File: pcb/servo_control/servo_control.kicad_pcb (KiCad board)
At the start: 2 copper layers, 23 parts, among them J1 USB_B_Micro, J10 Conn_01x03_Female, J11 Conn_01x03_Female, J12 Conn_01x03_Female, J13 Conn_01x03_Female, J14 Conn_01x03_Female, J15 Conn_01x03_Female, J16 Conn_01x03_Female, J17 Conn_01x03_Female, J18 Conn_01x03_Female, J19 Conn_01x03_Female, J2 Conn_02x03_Counter_Clockwise, J20 Conn_01x03_Female, J3 Conn_01x03_Female, J4 Conn_01x03_Female, J5 Conn_01x03_Female, J6 Conn_01x03_Female, J7 Conn_01x03_Female, J8 Conn_01x03_Female, J9 Conn_01x03_Female, U1 ATmega2560-16A, U2 MCP73832-2-OT

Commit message: add ftdi
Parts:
- added C1: 1 uf, Capacitor_SMD:C_0603_1608Metric, F.Cu at (109.2, 83.8)
- added C2: 1uf, Capacitor_SMD:C_0603_1608Metric, F.Cu at (119.4, 78.7)
- added C3: 10 uf, Capacitor_SMD:C_0603_1608Metric, F.Cu at (119.4, 81.3)
- added U3: ESP32-WROOM-32, ESP32:MODULE_ESP32-WROOM-32, F.Cu at (106.7, 63.5)
- U2: value MCP73832-2-OT -> LM317_SOT-223; footprint Package_TO_SOT_SMD:SOT-23-5 -> Package_TO_SOT_SMD:SOT-223-3_TabPin2
- moved U2 76.1 mm to (112.4, 78.7)
- moved J12 66.5 mm to (182.6, 96.8)
- moved J7 66.3 mm to (147.3, 43.2)
- moved J13 65.2 mm to (185.2, 96.8)
- moved J10 54.0 mm to (185.4, 43.2)
- moved J9 53.3 mm to (182.9, 43.2)
- moved D1 53.1 mm to (102.3, 75.2), turned to 180 degrees
- moved J14 51.8 mm to (187.7, 96.8)
- moved J18 32.7 mm to (149.8, 96.8)
- moved J15 31.9 mm to (104.1, 96.5)
- moved J17 31.4 mm to (109.2, 96.5)
- moved J2 30.9 mm to (132.1, 86.4), turned to 90 degrees
- moved J8 25.1 mm to (149.9, 43.2)
- moved U1 24.4 mm to (147.3, 73.7)
- moved J20 23.0 mm to (144.8, 96.8)
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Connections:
- net MISO renamed GPIO_50
- net SCK renamed GPIO_52
- J10 pad 3: unconnected-(J10-Pad3) -> GPIO_33
- J11 pad 3: unconnected-(J11-Pad3) -> GPIO_35
- J12 pad 3: unconnected-(J12-Pad3) -> GPIO_37
- J13 pad 3: unconnected-(J13-Pad3) -> GPIO_39
- J14 pad 3: unconnected-(J14-Pad3) -> GPIO_41
- J15 pad 3: unconnected-(J15-Pad3) -> GPIO_49
- J16 pad 3: unconnected-(J16-Pad3) -> GPIO_51
- J17 pad 3: unconnected-(J17-Pad3) -> GPIO_53
- J18 pad 3: unconnected-(J18-Pad3) -> GPIO_43
- J19 pad 3: unconnected-(J19-Pad3) -> GPIO_45
- J2 pad 5: MOSI -> GPIO_51
- J20 pad 3: unconnected-(J20-Pad3) -> GPIO_47
- J9 pad 3: unconnected-(J9-Pad3) -> GPIO_31
- U1 pad 11: Net-(U1-Pad11) -> GND
- U1 pad 21: MOSI -> GPIO_51
- U1 pad 32: Net-(U1-Pad11) -> GND
- U1 pad 43: unconnected-(U1-Pad43) -> GPIO_21
- U1 pad 44: unconnected-(U1-Pad44) -> GPIO_20
- U1 pad 45: unconnected-(U1-Pad45) -> GPIO_19
- U1 pad 46: unconnected-(U1-Pad46) -> GPIO_18
- U1 pad 50: unconnected-(U1-Pad50) -> GPIO_38
- U1 pad 53: unconnected-(U1-Pad53) -> GPIO_37
- U1 pad 54: unconnected-(U1-Pad54) -> GPIO_36
- U1 pad 55: unconnected-(U1-Pad55) -> GPIO_35
- U1 pad 56: unconnected-(U1-Pad56) -> GPIO_34
- U1 pad 57: unconnected-(U1-Pad57) -> GPIO_33
- U1 pad 58: unconnected-(U1-Pad58) -> GPIO_32
- U1 pad 59: unconnected-(U1-Pad59) -> GPIO_31
- U1 pad 60: unconnected-(U1-Pad60) -> GPIO_30
- U1 pad 62: Net-(U1-Pad11) -> GND
- U1 pad 81: Net-(U1-Pad11) -> GND
- U1 pad 82: unconnected-(U1-Pad82) -> GPIO_15
- U1 pad 83: unconnected-(U1-Pad83) -> GPIO_14
- U1 pad 84: unconnected-(U1-Pad84) -> GPIO_13
- U1 pad 85: unconnected-(U1-Pad85) -> GPIO_12
- U1 pad 86: unconnected-(U1-Pad86) -> GPIO_11
- U1 pad 87: unconnected-(U1-Pad87) -> GPIO_10
- U1 pad 88: unconnected-(U1-Pad88) -> GPIO_9
- U1 pad 89: unconnected-(U1-Pad89) -> GPIO_8
- U1 pad 90: unconnected-(U1-Pad90) -> GPIO_7
- U1 pad 91: unconnected-(U1-Pad91) -> GPIO_6
- U1 pad 92: unconnected-(U1-Pad92) -> GPIO_5
- U1 pad 93: unconnected-(U1-Pad93) -> GPIO_4
- U1 pad 94: unconnected-(U1-Pad94) -> GPIO_3
- U1 pad 95: unconnected-(U1-Pad95) -> GPIO_2
- U1 pad 96: unconnected-(U1-Pad96) -> GPIO_1
- U1 pad 97: unconnected-(U1-Pad97) -> GPIO_0
- U1 pad 99: Net-(U1-Pad11) -> GND
- U2 pad 1: unconnected-(U2-Pad1) -> GND
- U2 pad 2: unconnected-(U2-Pad2) -> 3.3V
- U2 pad 3: unconnected-(U2-Pad3) -> VCC

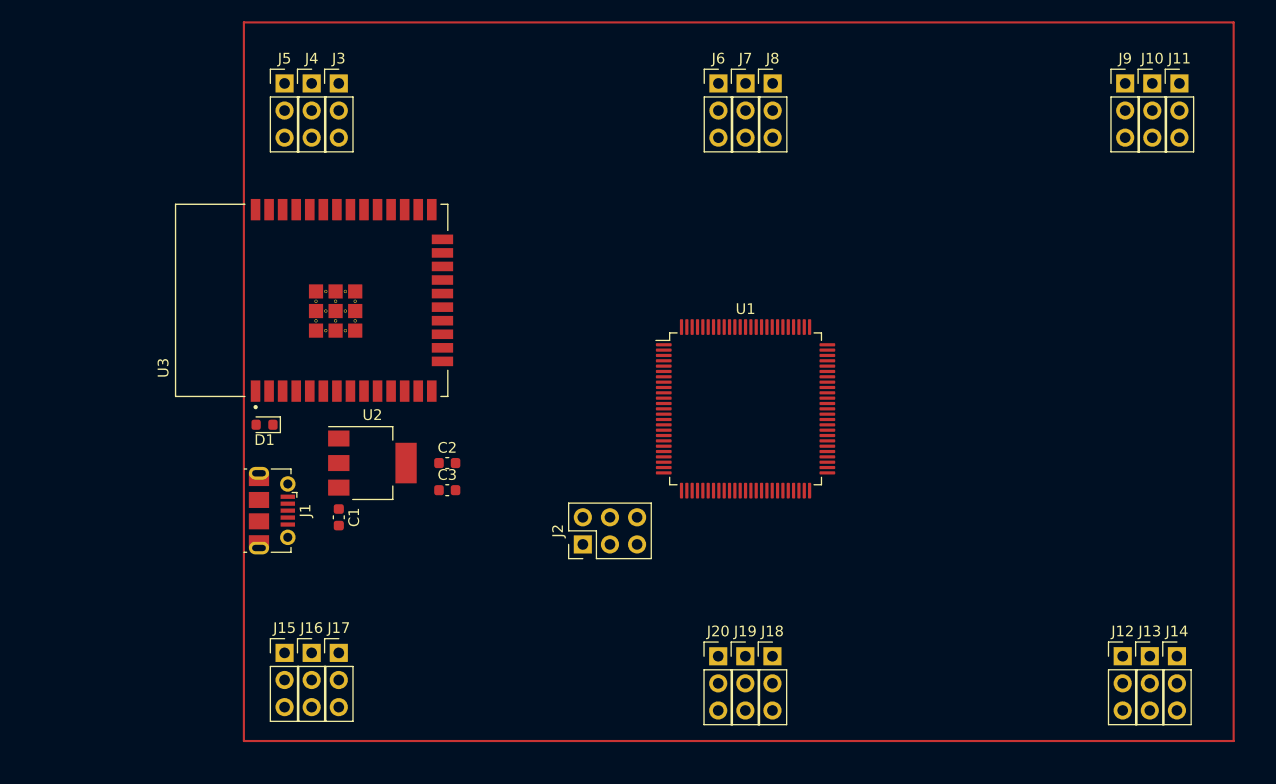
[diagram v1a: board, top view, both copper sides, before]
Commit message: add i2c
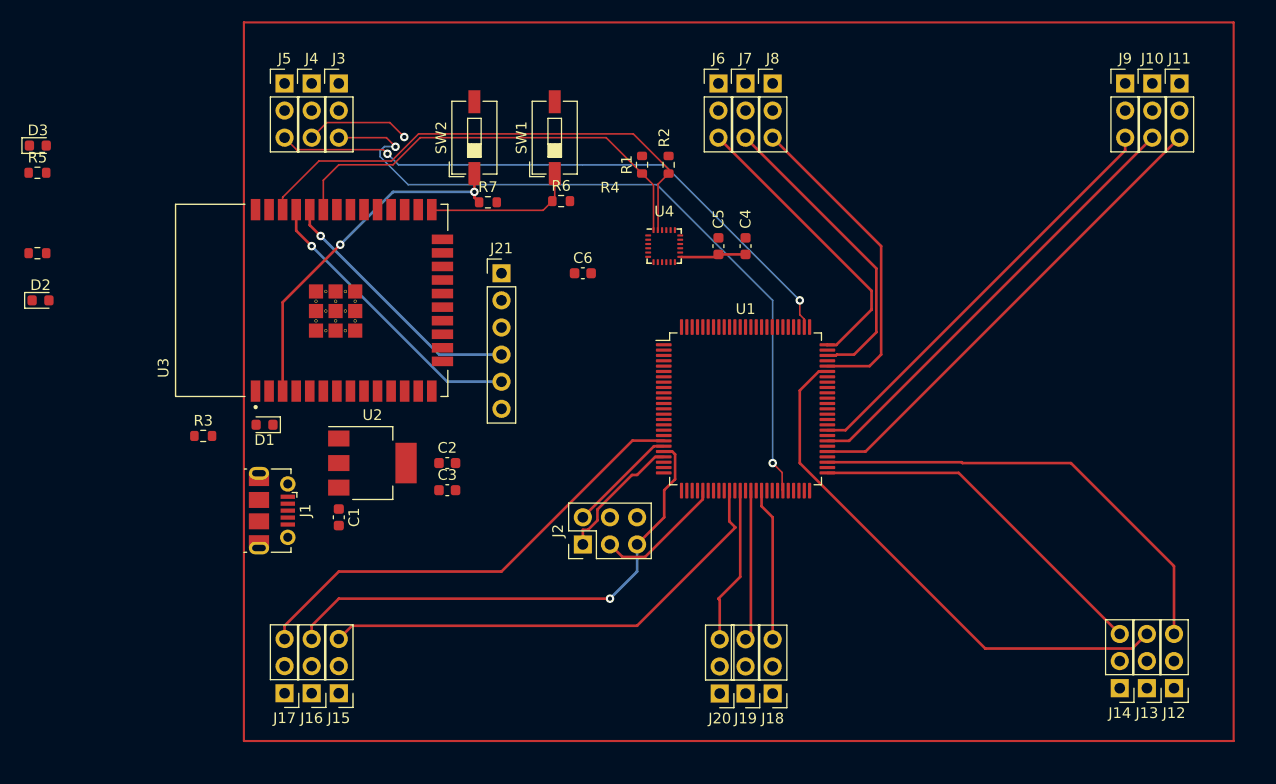
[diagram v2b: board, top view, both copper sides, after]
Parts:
- added C4: 10 nf, Capacitor_SMD:C_0603_1608Metric, F.Cu at (147.3, 58.4)
- added C5: 0.1 uf, Capacitor_SMD:C_0603_1608Metric, F.Cu at (144.8, 58.4)
- added C6: 0.1 uf, Capacitor_SMD:C_0603_1608Metric, F.Cu at (132.1, 61.0)
- added D2: LED, LED_SMD:LED_0603_1608Metric, F.Cu at (81.3, 63.5)
- added D3: LED, LED_SMD:LED_0603_1608Metric, F.Cu at (81.0, 49.0)
- added J21: Conn_01x06_Male, Connector_PinHeader_2.54mm:PinHeader_1x06_P2.54mm_Vertical, F.Cu at (124.5, 61.0)
- added R1: 4.7K, Resistor_SMD:R_0603_1608Metric, F.Cu at (137.6, 50.8)
- added R2: 4.7K, Resistor_SMD:R_0603_1608Metric, F.Cu at (140.1, 50.8)
- added R3: 1K, Resistor_SMD:R_0603_1608Metric, F.Cu at (96.5, 76.2)
- added R4: 1K, Resistor_SMD:R_0603_1608Metric, F.Cu at (81.0, 59.1)
- added R5: 1K, Resistor_SMD:R_0603_1608Metric, F.Cu at (81.0, 51.5)
- added R6: 10K, Resistor_SMD:R_0603_1608Metric, F.Cu at (130.0, 54.2)
- added R7: 10K, Resistor_SMD:R_0603_1608Metric, F.Cu at (123.2, 54.3)
- added SW1: ESP_PROG, Button_Switch_SMD:SW_DIP_SPSTx01_Slide_6.7x4.1mm_W6.73mm_P2.54mm_LowProfile_JPin, F.Cu at (129.4, 48.3)
- added SW2: ESP_RST, Button_Switch_SMD:SW_DIP_SPSTx01_Slide_6.7x4.1mm_W6.73mm_P2.54mm_LowProfile_JPin, F.Cu at (121.9, 48.3)
- added U4: MPU-9250, Sensor_Motion:InvenSense_QFN-24_3x3mm_P0.4mm, F.Cu at (139.7, 58.4)
- moved J15 6.33 mm to (109.2, 100.3), turned to 180 degrees
- moved J17 6.33 mm to (104.1, 100.3), turned to 180 degrees
- moved J14 6.14 mm to (182.4, 99.8), turned to 180 degrees
- moved J12 5.66 mm to (187.5, 99.8), turned to 180 degrees
- moved J16 3.78 mm to (106.7, 100.3), turned to 180 degrees
- moved J20 3.50 mm to (144.9, 100.3), turned to 180 degrees
- moved J18 3.50 mm to (149.9, 100.3), turned to 180 degrees
- moved J19 3.50 mm to (147.3, 100.3), turned to 180 degrees
- moved J13 3.01 mm to (184.9, 99.8), turned to 180 degrees
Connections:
- D1 pad 1: unconnected-(D1-Pad1) -> GND
- D1 pad 2: unconnected-(D1-Pad2) -> Net-(D1-Pad2)
- J1 pad 6: unconnected-(J1-Pad6) -> GND
- U1 pad 35: unconnected-(U1-Pad35) -> GPIO_49
- U1 pad 36: unconnected-(U1-Pad36) -> GPIO_48
- U1 pad 37: unconnected-(U1-Pad37) -> GPIO_47
- U1 pad 38: unconnected-(U1-Pad38) -> GPIO_46
- U1 pad 39: unconnected-(U1-Pad39) -> GPIO_45
- U1 pad 40: unconnected-(U1-Pad40) -> GPIO_44
- U1 pad 41: unconnected-(U1-Pad41) -> GPIO_43
- U1 pad 42: unconnected-(U1-Pad42) -> GPIO_42
- U1 pad 43: GPIO_21 -> I2C_SCL
- U1 pad 44: GPIO_20 -> I2C_SDA
- U1 pad 51: unconnected-(U1-Pad51) -> GPIO_41
- U1 pad 52: unconnected-(U1-Pad52) -> GPIO_40
- U1 pad 70: unconnected-(U1-Pad70) -> GPIO_39
- U3 pad 2: unconnected-(U3-Pad2) -> 3.3V
- U3 pad 25: unconnected-(U3-Pad25) -> Net-(U3-Pad25)
- U3 pad 3: unconnected-(U3-Pad3) -> Net-(U3-Pad3)
- U3 pad 33: unconnected-(U3-Pad33) -> I2C_SDA
- U3 pad 34: unconnected-(U3-Pad34) -> FTDI_TX
- U3 pad 35: unconnected-(U3-Pad35) -> FTDI_RX
- U3 pad 36: unconnected-(U3-Pad36) -> I2C_SCL
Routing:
- net GPIO_19: track 0.00 -> 68.4 mm, vias 0 -> 2
- net GPIO_23: track 0.00 -> 57.2 mm, vias 0 -> 2
- net GPIO_39: track 0.00 -> 50.4 mm
- net GPIO_51: track 0.00 -> 47.4 mm, vias 0 -> 1
- net I2C_SCL: track 0.00 -> 47.3 mm
- net GPIO_49: track 0.00 -> 45.3 mm
- net GPIO_35: track 0.00 -> 45.2 mm
- net GPIO_53: track 0.00 -> 44.0 mm
- net GPIO_37: track 0.00 -> 42.9 mm
- net GPIO_33: track 0.00 -> 42.2 mm
- net I2C_SDA: track 0.00 -> 41.4 mm
- net GPIO_31: track 0.00 -> 40.0 mm
- net GPIO_41: track 0.00 -> 33.6 mm
- net Net-(U3-Pad3): track 0.00 -> 33.4 mm, vias 0 -> 2
- net GPIO_29: track 0.00 -> 30.0 mm
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
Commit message: add track vcc servo
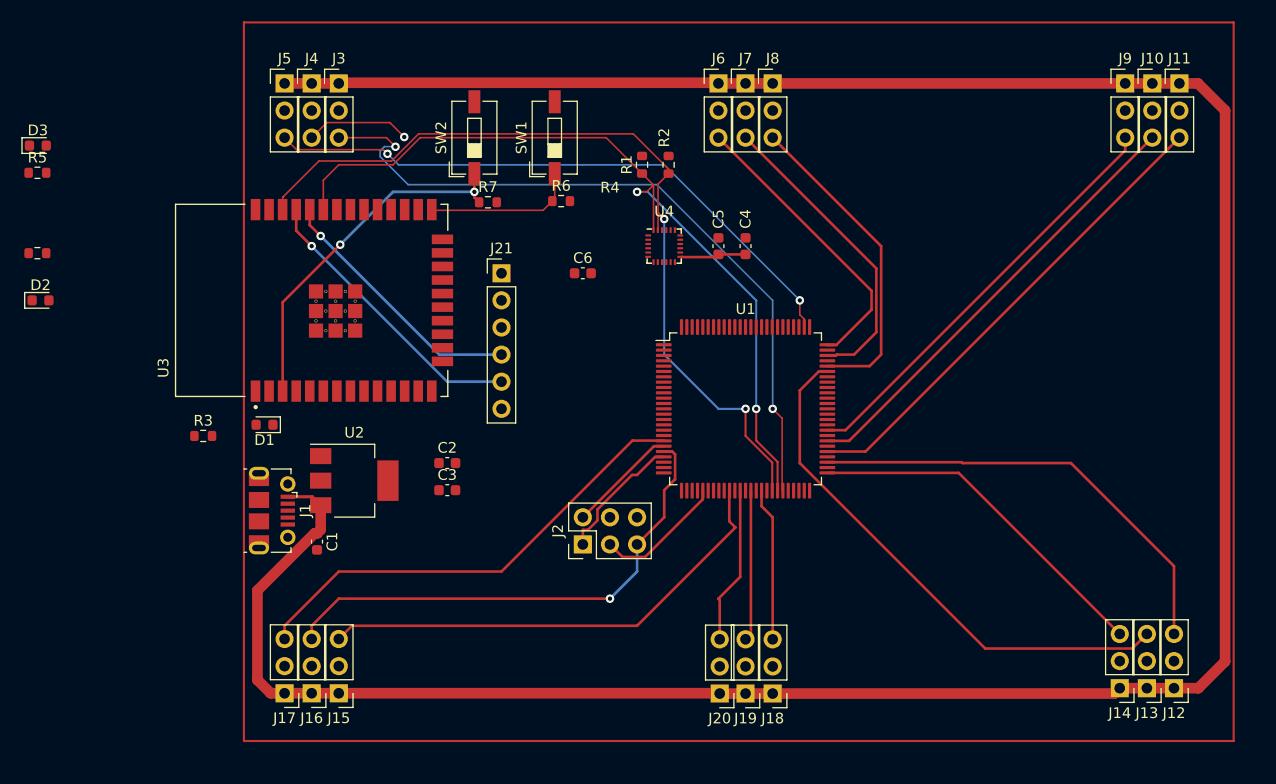
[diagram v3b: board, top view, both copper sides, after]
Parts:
- moved C1 3.06 mm to (107.2, 86.1)
- moved U2 2.36 mm to (110.7, 80.4)
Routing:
- net VCC: track 0.00 -> 255.6 mm
- net I2C_SDA: track 41.4 -> 77.2 mm, vias 0 -> 2
- net I2C_SCL: track 47.3 -> 79.2 mm, vias 0 -> 2

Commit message: add gnd zone
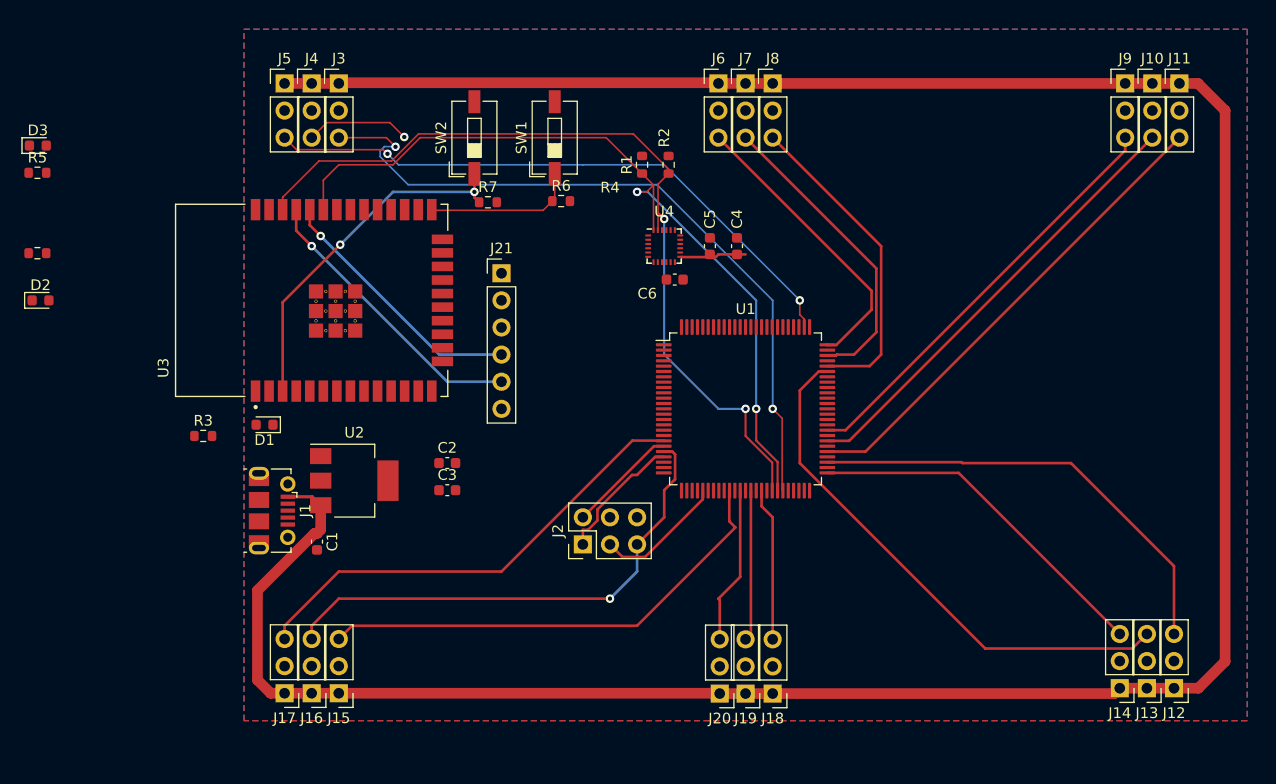
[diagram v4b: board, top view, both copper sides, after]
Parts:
- moved C6 8.63 mm to (140.7, 61.6)
- moved C5 0.80 mm to (144.0, 58.4)
- moved C4 0.80 mm to (146.5, 58.4)
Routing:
- added copper zone on B.Cu, net GND
- added copper zone on F.Cu, net GND
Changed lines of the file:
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@@
   )
   (footprint "Capacitor_SMD:C_0603_1608Metric" (layer "F.Cu")
-    (at 147.32 58.42 90)
+    (at 146.52 58.42 90)
     (descr "Capacitor SMD 0603 (1608 Metric), square (rectangular) end terminal, IPC_7351 nominal, (Body size source: IPC-SM-782 page 76, https://www.pcb-3d.com/wordpress/wp-content/uploads/ipc-sm-782a_amendment_1_and_2.pdf), generated with kicad-footprint-generator")
     (tags "capacitor")
@@
   )
   (footprint "Capacitor_SMD:C_0603_1608Metric" (layer "F.Cu")
-    (at 132.08 60.96)
+    (at 140.692384 61.553412)
     (descr "Capacitor SMD 0603 (1608 Metric), square (rectangular) end terminal, IPC_7351 nominal, (Body size source: IPC-SM-782 page 76, https://www.pcb-3d.com/wordpress/wp-content/uploads/ipc-sm-782a_amendment_1_and_2.pdf), generated with kicad-footprint-generator")
     (tags "capacitor")
@@
     (property "Sheetname" "")
     (attr smd)
-    (fp_text reference "C6" (at 0 -1.43) (layer "F.SilkS")
-      (effects (font (size 1 1) (thickness 0.15)))
-    )
-    (fp_text value "0.1 uf" (at 0 1.79) (layer "F.Fab")
+    (fp_text reference "C6" (at -2.583816 1.310452) (layer "F.SilkS")
+      (effects (font (size 1 1) (thickness 0.15)))
+    )
+    (fp_text value "0.1 uf" (at -3.894268 0.049451) (layer "F.Fab")
       (effects (font (size 1 1) (thickness 0.15)))
     )
@@
   )
   (footprint "Capacitor_SMD:C_0603_1608Metric" (layer "F.Cu")
-    (at 144.78 58.42 90)
+    (at 143.98 58.42 90)
     (descr "Capacitor SMD 0603 (1608 Metric), square (rectangular) end terminal, IPC_7351 nominal, (Body size source: IPC-SM-782 page 76, https://www.pcb-3d.com/wordpress/wp-content/uploads/ipc-sm-782a_amendment_1_and_2.pdf), generated with kicad-footprint-generator")
     (tags "capacitor")
@@
       (effects (font (size 1 1) (thickness 0.15)))
     )
-    (fp_text value "MPU-9250" (at 0 3.25) (layer "F.Fab")
+    (fp_text value "MPU-9250" (at -6.239828 0) (layer "F.Fab")
       (effects (font (size 1 1) (thickness 0.15)))
     )
@@
     )
   )
-  (gr_rect (start 100.33 37.465) (end 193.04 104.775) (layer "F.Cu") (width 0.2) (fill none))
   (segment (start 138.854315 78.16) (end 139.6575 78.16) (width 0.25) (layer "F.Cu") (net 14))
   (segment (start 132.566701 84.995) (end 133.445 84.116701) (width 0.25) (layer "F.Cu") (net 14))
@@
   (segment (start 109.357224 58.282776) (end 114.3 53.34) (width 0.25) (layer "B.Cu") (net 142))
   (segment (start 114.3 53.34) (end 121.92 53.34) (width 0.25) (layer "B.Cu") (net 142))
+  (zone (net 4) (net_name "GND") (layers F&B.Cu) (hatch edge 0.508)
+    (connect_pads (clearance 0.508))
+    (min_thickness 0.254) (filled_areas_thickness no)
+    (fill yes (thermal_gap 0.508) (thermal_bridge_width 0.508))
+    (polygon
+      (pts
+        (xy 194.31 102.87)
+        (xy 100.33 102.87)
+        (xy 100.33 38.1)
+        (xy 194.31 38.1)
+      )
+    )
+  )
 )
